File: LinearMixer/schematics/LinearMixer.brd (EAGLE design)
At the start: 100 x 61 mm, 70 parts, among them IC1 NE5532D, IC2 NE5532D, IC3 NE5532D, IC4 QUAD_OPAMPD, IC5 QUAD_OPAMPD, IC6 QUAD_OPAMPD, IC7 QUAD_OPAMPD, IC8 SSM2164P

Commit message: renamed InvertingMixer
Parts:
- removed C3, C4: 100p, resistor:C0603
- removed C301, C302, C5, C6: 100n, resistor:C0603
- removed D3: (no value), adafruit:DO35-7
- removed IC3: NE5532D, linear:SO08
- removed IC4, IC5, IC6, IC7: QUAD_OPAMPD, adafruit:SO14
- removed IC8: SSM2164P, ssm2164:DIL16
- removed IN_CV_A, IN_CV_B, OUT_A, OUT_B: JACK-PJ-301B, Rebel:PJ-301B
- removed JP_IN, JP_SW_IN: (no value), adafruit:2X04
- removed JP_IN5: (no value), SparkFun:1X02
- removed R13, R34, R35, R8: 30k, resistor:R0603
- removed R17, R18: 100k, resistor:R0603
- removed R25: 100R, resistor:R0603
- removed R27: 100r, resistor:R0603
- removed R3: 6K, resistor:R0603
- removed R7: 100K, resistor:R0603
- added JP1: (no value), pinhead:1X02
- added OUT_A+, OUT_A-, OUT_B+, OUT_B-: JACK-PJ-301B, Rebel:PJ-301B
- added R104, R105, R205: 100k, resistor:R0603
- added R106, R107, R108, R206, R207, R208: (no value), resistor:R0603
- added R110, R210: 100R, resistor:R0603
- added X1, X2: 53048-05, con-molex:53048-05
- added X3, X4, X5: 53048-03, con-molex:53048-03
- C1, C2: device resistor:PANASONIC_A -> rcl:153CLV-0505
- IC1, IC2: value NE5532D -> QUAD_OPAMPD; device linear:SO08 -> adafruit:SO14
- R1, R2: value 100K -> 10k
- R109, R209: value 100k -> 100R
- moved R2 301.2 mm to (4.45, 36.8)
- moved R1 299.3 mm to (4.45, 42.5), turned to 180 degrees
- moved R201 282.9 mm to (39.4, 86.4), turned to 180 degrees
- moved R101 266.9 mm to (14.0, 86.4), turned to 180 degrees
- moved R202 263.4 mm to (39.4, 67.3), turned to 180 degrees
- moved R102 262.6 mm to (14.0, 66.0), turned to 180 degrees
- moved R109 251.8 mm to (22.9, 55.9), turned to 180 degrees
- moved R203 251.1 mm to (39.4, 47.0)
- moved R103 244.5 mm to (15.2, 48.3), turned to 180 degrees
- moved R209 238.8 mm to (29.2, 38.1), turned to 180 degrees
- moved R204 232.4 mm to (39.4, 29.2), turned to 180 degrees
- moved R501 218.7 mm to (33.0, 68.6)
- moved R504 214.9 mm to (20.3, 68.6), turned to 180 degrees
- moved R502 214.4 mm to (33.0, 65.4)
- moved R503 212.1 mm to (20.3, 65.4), turned to 180 degrees
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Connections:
- removed net CV_IN: IN_CV_A.TIP, R7.2
- removed net N$12: IC8.1, R3.2
- removed net N$62: JP_IN5.1, R209.2
- removed net N$8: R2.2
- removed net V+: IC1.8, IC2.8, IC3.8, IC7.4
- removed net V-: IC1.4, IC2.4, IC3.4, IC7.11
- new net N$11: OUT_A-.TIP, R109.2
- new net N$17: OUT_B-.TIP, R209.2
- net +12V: now also IC1.4, IC2.4, R1.1, X5.3; no longer C301.1, C5.1, IC4.4, IC5.4, IC6.4, IC8.16, R3.1
- net -12V: now also IC1.11, IC2.11, X5.1; no longer C302.1, C6.2, D3.A, IC4.11, IC5.11, IC6.11, IC8.9, R1.1
- net GND: now also IC1.10, IC1.12, IC1.3, OUT_A+.SHL, OUT_A+.SLV, OUT_A-.SHL, OUT_A-.SLV, OUT_B+.SHL, OUT_B+.SLV, OUT_B-.SHL, OUT_B-.SLV, POT1A.P$5, POT1A.P$6, POT1B.P$5, POT1B.P$6, POT2A.P$5, POT2A.P$6, POT2B.P$5, POT2B.P$6, POT3A.P$5, POT3A.P$6, POT3B.P$5, POT3B.P$6, POT4A.P$5, POT4A.P$6, POT4B.P$5, POT4B.P$6, R2.2, X1.3, X2.3, X3.2, X4.2, X5.2; no longer C301.2, C302.2, C4.1, C5.2, C6.1, D3.C, IC2.3, IC2.5, IC3.3, IC3.5, IC8.8, OUT_A.SHL, OUT_A.SLV, OUT_B.SHL, OUT_B.SLV
- net N$1: now also IC1.1, R106.2, R107.1, R109.1; no longer IC2.1, R17.2, R34.1
- net N$14: now also IC1.8, R206.2, R207.1, R209.1; no longer IC2.7, R18.2, R35.1
- net N$15: now also OUT_B+.TIP, R210.2; no longer OUT_B.TIP, R27.2
- net N$18: now also IC1.6, R107.2, R108.1; no longer IC3.2, R34.2, R8.1
- net N$2: now also R205.2, X3.3; no longer C3.2, IC1.7, IC8.3, IC8.6
- net N$23: now also IC1.13, R207.2, R208.1; no longer IC3.6, R13.1, R35.2
- net N$27: now also IC2.8, IC2.9; no longer IC7.8, IC7.9
- net N$3: now also OUT_A+.SW, X4.3; no longer C3.1, IC1.6, IC8.4, R7.1
- net N$33: now also X2.1; no longer JP_IN.7, JP_IN.8
- net N$34: now also IC2.13, IC2.14; no longer IC7.13, IC7.14
- net N$35: now also X2.5; no longer JP_IN.1, JP_IN.2
- net N$36: now also X2.4; no longer JP_IN.3, JP_IN.4
- net N$37: now also X2.2; no longer JP_IN.5, JP_IN.6
- net N$38: now also X1.1; no longer JP_SW_IN.1, JP_SW_IN.2
- net N$39: now also X1.2; no longer JP_SW_IN.3, JP_SW_IN.4
- net N$4: now also OUT_B+.SW, X4.1; no longer C4.2, IC8.2, R1.2
- net N$40: now also X1.4; no longer JP_SW_IN.5, JP_SW_IN.6
- net N$41: now also JP1.2, X1.5; no longer JP_SW_IN.7, JP_SW_IN.8
- net N$42: now also IC2.3; no longer IC7.3
- net N$43: now also IC2.5; no longer IC7.5
- net N$47: now also R104.2
- net N$48: now also IC2.10; no longer IC7.10
- net N$5: now also IC1.14, R208.2, R210.1; no longer IC3.7, R13.2, R27.1
- net N$50: now also IC2.12; no longer IC7.12
- net N$52: now also IC1.2, R104.1, R105.1, R106.1; no longer IC2.2, R109.1, R17.1
- net N$53: now also IC2.6, IC2.7; no longer IC7.6, IC7.7
- net N$58: now also IC2.1, IC2.2; no longer IC7.1, IC7.2
- net N$6: now also IC1.7, R108.2, R110.1; no longer IC3.1, R25.1, R8.2
- net N$61: now also IC1.9, R205.1, R206.1; no longer IC2.6, R18.1, R209.1
- net N$63: now also R105.2, X3.1; no longer JP_IN5.2, R109.2
- net N$7: now also JP1.1, R1.2; no longer IC8.7
- net N$9: now also OUT_A+.TIP, R110.2; no longer OUT_A.TIP, R25.2
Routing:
- net N$61: track 0.00 -> 133.3 mm, vias 0 -> 6
- net +12V: track 0.00 -> 114.6 mm, vias 0 -> 9
- net N$33: track 0.00 -> 99.8 mm, vias 0 -> 2
- net N$52: track 0.00 -> 85.3 mm, vias 0 -> 5
- net -12V: track 0.00 -> 83.9 mm, vias 0 -> 7
- net N$3: track 0.00 -> 78.2 mm
- net N$35: track 0.00 -> 76.6 mm, vias 0 -> 2
- net N$58: track 0.00 -> 76.2 mm, vias 0 -> 2
- net N$15: track 0.00 -> 71.2 mm, vias 0 -> 2
- net N$37: track 0.00 -> 71.0 mm, vias 0 -> 3
- net N$11: track 0.00 -> 70.6 mm, vias 0 -> 1
- net N$36: track 0.00 -> 69.0 mm, vias 0 -> 4
- net N$38: track 0.00 -> 54.6 mm, vias 0 -> 1
- net N$34: track 0.00 -> 53.4 mm, vias 0 -> 2
- net N$53: track 0.00 -> 52.8 mm, vias 0 -> 2
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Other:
- board size 100 x 61 mm -> 50.3 x 100 mm
- board text added: "LinearMixer Rev01"
- board text added: "Rebel Technology"

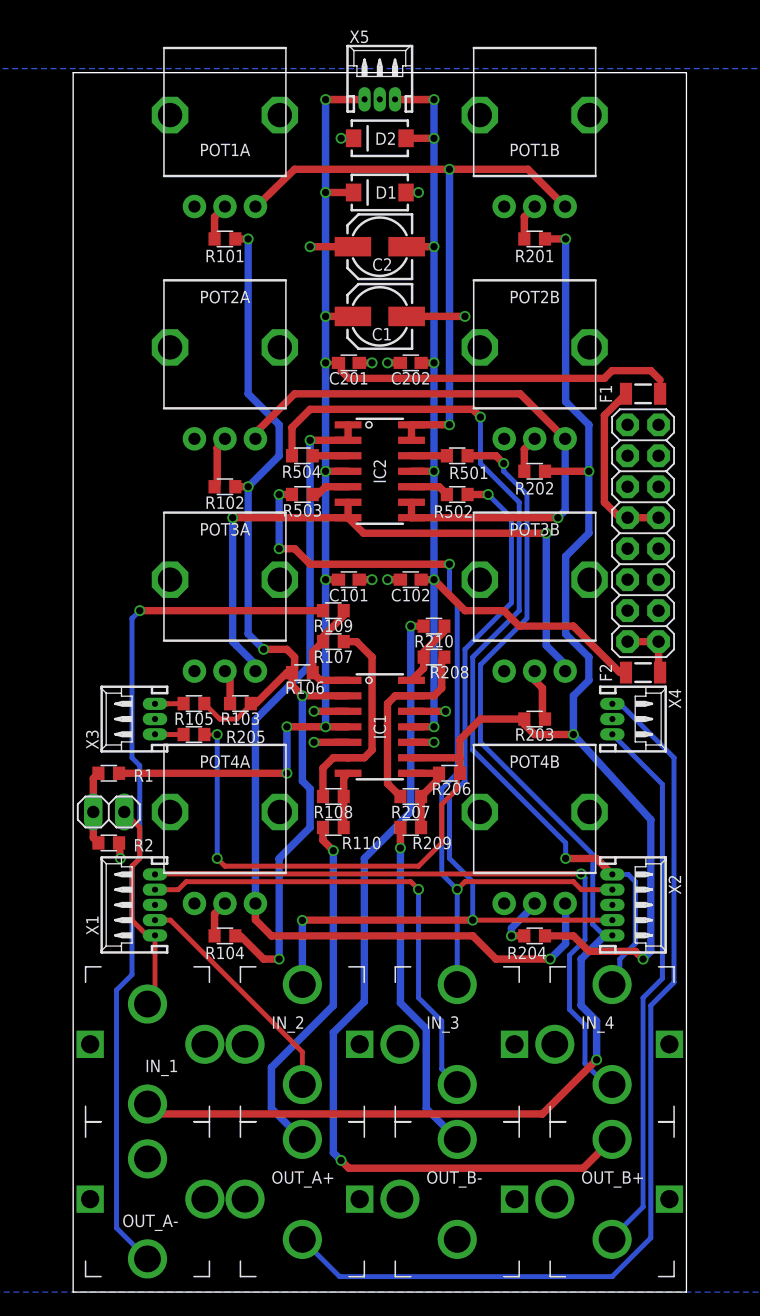
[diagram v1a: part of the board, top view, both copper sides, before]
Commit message: named input and output nets
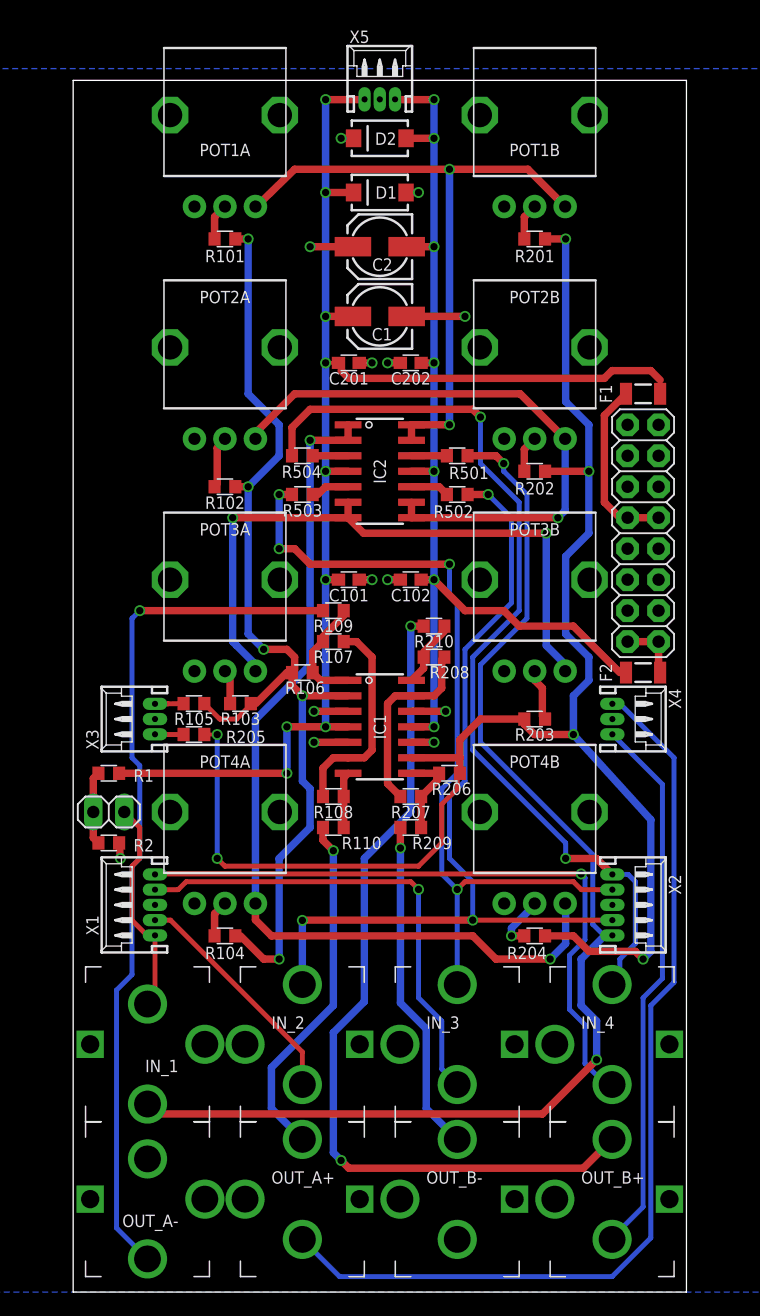
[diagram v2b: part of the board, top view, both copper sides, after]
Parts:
- R106, R206: value (none) -> 200k
- R107, R108, R207, R208: value (none) -> 100k
- R501, R502, R503, R504: value 100k -> 1k
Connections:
- net N$2 renamed IN_B
- net N$3 renamed OUT_SW_A
- net N$33 renamed IN_1
- net N$35 renamed IN_4
- net N$36 renamed IN_3
- net N$37 renamed IN_2
- net N$38 renamed IN_SW_4
- net N$39 renamed IN_SW_3
- net N$4 renamed OUT_SW_B
- net N$40 renamed IN_SW_2
- net N$41 renamed IN_SW_1
- net N$63 renamed IN_A
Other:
- board size 50.3 x 100 mm -> 50.3 x 99.4 mm
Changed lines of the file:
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@@
 <board>
 <plain>
-<wire x1="51.816" y1="0" x2="51.816" y2="100" width="0" layer="20"/>
-<wire x1="51.816" y1="100" x2="1.524" y2="100" width="0" layer="20"/>
-<wire x1="1.524" y1="100" x2="1.524" y2="0" width="0" layer="20"/>
+<wire x1="51.816" y1="0" x2="51.816" y2="99.365" width="0" layer="20"/>
+<wire x1="51.816" y1="99.365" x2="1.524" y2="99.365" width="0" layer="20"/>
+<wire x1="1.524" y1="99.365" x2="1.524" y2="0" width="0" layer="20"/>
 <wire x1="1.524" y1="0" x2="51.816" y2="0" width="0" layer="20"/>
 <dimension x1="1.27" y1="0" x2="1.27" y2="100" x3="-1.27" y3="50" textsize="1.778" layer="47"/>
-<dimension x1="1.905" y1="0" x2="51.435" y2="0" x3="26.67" y3="-3.81" textsize="1.778" layer="47"/>
-<dimension x1="1.524" y1="0" x2="51.816" y2="0" x3="26.67" y3="-5.715" textsize="1.778" layer="47"/>
+<dimension x1="1.524" y1="0" x2="51.816" y2="0" x3="26.67" y3="-4.445" textsize="1.778" layer="47"/>
 <text x="4.445" y="64.135" size="1.778" layer="47" font="vector" rot="R90">Rebel Technology</text>
 <text x="6.985" y="64.135" size="1.778" layer="47" font="vector" rot="R90">LinearMixer Rev01</text>
@@
 </autorouter>
 <elements>
-<element name="R108" library="resistor" package="R0603" value="" x="22.86" y="40.64" smashed="yes">
+<element name="R108" library="resistor" package="R0603" value="100k" x="22.86" y="40.64" smashed="yes">
 <attribute name="NAME" x="22.86" y="39.878" size="1.016" layer="25" font="vector" rot="R180" align="bottom-center"/>
 </element>
-<element name="R208" library="resistor" package="R0603" value="" x="31.115" y="52.07" smashed="yes" rot="R180">
+<element name="R208" library="resistor" package="R0603" value="100k" x="31.115" y="52.07" smashed="yes" rot="R180">
 <attribute name="NAME" x="32.385" y="51.33975" size="1.016" layer="25" font="vector" rot="R180" align="bottom-center"/>
 </element>
-<element name="R106" library="resistor" package="R0603" value="" x="20.32" y="50.8" smashed="yes">
+<element name="R106" library="resistor" package="R0603" value="200k" x="20.32" y="50.8" smashed="yes">
 <attribute name="NAME" x="20.54225" y="50.06975" size="1.016" layer="25" font="vector" rot="R180" align="bottom-center"/>
 </element>
-<element name="R206" library="resistor" package="R0603" value="" x="32.385" y="42.545" smashed="yes" rot="R180">
+<element name="R206" library="resistor" package="R0603" value="200k" x="32.385" y="42.545" smashed="yes" rot="R180">
 <attribute name="NAME" x="32.54375" y="41.783" size="1.016" layer="25" font="vector" rot="R180" align="bottom-center"/>
 </element>
-<element name="R107" library="resistor" package="R0603" value="" x="22.86" y="53.34" smashed="yes">
+<element name="R107" library="resistor" package="R0603" value="100k" x="22.86" y="53.34" smashed="yes">
 <attribute name="NAME" x="22.86" y="52.60975" size="1.016" layer="25" font="vector" rot="R180" align="bottom-center"/>
 </element>
-<element name="R207" library="resistor" package="R0603" value="" x="29.21" y="40.64" smashed="yes" rot="R180">
+<element name="R207" library="resistor" package="R0603" value="100k" x="29.21" y="40.64" smashed="yes" rot="R180">
 <attribute name="NAME" x="29.21" y="39.878" size="1.016" layer="25" font="vector" rot="R180" align="bottom-center"/>
 </element>
@@
 <attribute name="NAME" x="26.162" y="67.31" size="1.016" layer="25" font="vector" rot="R270" align="bottom-center"/>
 </element>
-<element name="R504" library="resistor" package="R0603" value="100k" x="20.32" y="68.58" smashed="yes" rot="R180">
+<element name="R504" library="resistor" package="R0603" value="1k" x="20.32" y="68.58" smashed="yes" rot="R180">
 <attribute name="NAME" x="20.2565" y="67.78625" size="1.016" layer="25" font="vector" rot="R180" align="bottom-center"/>
 </element>
-<element name="R503" library="resistor" package="R0603" value="100k" x="20.32" y="65.405" smashed="yes" rot="R180">
+<element name="R503" library="resistor" package="R0603" value="1k" x="20.32" y="65.405" smashed="yes" rot="R180">
 <attribute name="NAME" x="20.32" y="64.61125" size="1.016" layer="25" font="vector" rot="R180" align="bottom-center"/>
 </element>
-<element name="R502" library="resistor" package="R0603" value="100k" x="33.02" y="65.405" smashed="yes">
+<element name="R502" library="resistor" package="R0603" value="1k" x="33.02" y="65.405" smashed="yes">
 <attribute name="NAME" x="32.7025" y="64.516" size="1.016" layer="25" font="vector" rot="R180" align="bottom-center"/>
 </element>
-<element name="R501" library="resistor" package="R0603" value="100k" x="33.02" y="68.58" smashed="yes">
+<element name="R501" library="resistor" package="R0603" value="1k" x="33.02" y="68.58" smashed="yes">
 <attribute name="NAME" x="33.9725" y="67.691" size="1.016" layer="25" font="vector" rot="R180" align="bottom-center"/>
 </element>
@@
 <wire x1="38.18" y1="73.66" x2="41.87" y2="69.97" width="0.6096" layer="1"/>
 </signal>
-<signal name="N$33">
+<signal name="IN_1">
 <contactref element="IN_1" pad="TIP"/>
 <contactref element="R501" pad="2"/>
@@
 <wire x1="38.815" y1="92.075" x2="41.87" y2="89.02" width="0.6096" layer="1"/>
 </signal>
-<signal name="N$35">
+<signal name="IN_4">
 <contactref element="IN_4" pad="TIP"/>
 <contactref element="R504" pad="2"/>
@@
 <wire x1="44.43" y1="35.56" x2="45.74" y2="34.25" width="0.6096" layer="1"/>
 </signal>
-<signal name="N$36">
+<signal name="IN_3">
 <contactref element="IN_3" pad="TIP"/>
 <contactref element="R503" pad="2"/>
@@
 <wire x1="31.75" y1="34.29" x2="33.02" y2="33.02" width="0.4064" layer="16"/>
 </signal>
-<signal name="N$37">
+<signal name="IN_2">
 <contactref element="IN_2" pad="TIP"/>
 <contactref element="R502" pad="2"/>
@@
 <via x="34.29" y="30.5" extent="1-16" drill="0.6"/>
 </signal>
-<signal name="N$38">
+<signal name="IN_SW_4">
 <contactref element="IN_4" pad="SW"/>
 <contactref element="X1" pad="1"/>
@@
 <wire x1="45.595" y1="17.145" x2="45.72" y2="17.02" width="0.4064" layer="16"/>
 </signal>
-<signal name="N$39">
+<signal name="IN_SW_3">
 <contactref element="IN_3" pad="SW"/>
 <contactref element="X1" pad="2"/>
@@
 <wire x1="31.75" y1="18.29" x2="33.02" y2="17.02" width="0.4064" layer="16"/>
 </signal>
-<signal name="N$40">
+<signal name="IN_SW_2">
 <contactref element="IN_2" pad="SW"/>
 <contactref element="X1" pad="4"/>
@@
 <wire x1="20.32" y1="19.685" x2="20.32" y2="17.02" width="0.4064" layer="1"/>
 </signal>
-<signal name="N$41">
+<signal name="IN_SW_1">
 <contactref element="IN_1" pad="SW"/>
 <contactref element="X1" pad="5"/>
@@
 <wire x1="39.37" y1="45.72" x2="38.52" y2="46.57" width="0.6096" layer="1"/>
 </signal>
-<signal name="N$63">
+<signal name="IN_A">
 <contactref element="R105" pad="2"/>
 <contactref element="X3" pad="1"/>
@@
 <wire x1="9.29" y1="48.24" x2="10.58" y2="48.26" width="0.4064" layer="1"/>
 </signal>
-<signal name="N$2">
+<signal name="IN_B">
 <contactref element="R205" pad="2"/>
 <contactref element="X3" pad="3"/>
@@
 <wire x1="8.255" y1="45.72" x2="8.235" y2="45.74" width="0.3048" layer="1"/>
 </signal>
-<signal name="N$3">
+<signal name="OUT_SW_A">
 <contactref element="OUT_A+" pad="SW"/>
 <wire x1="50.8" y1="43.815" x2="50.8" y2="25.4" width="0.4064" layer="16"/>
@@
 <wire x1="46.375" y1="48.24" x2="50.8" y2="43.815" width="0.4064" layer="16"/>
 </signal>
-<signal name="N$4">
+<signal name="OUT_SW_B">
 <contactref element="OUT_B+" pad="SW"/>
 <contactref element="X4" pad="1"/>
